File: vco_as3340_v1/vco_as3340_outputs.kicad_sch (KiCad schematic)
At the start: 27 parts, among them J4 TRIANGLE, J5 SAWTOOTH, J6 PULSE, U4 TL072, U5 TL072, U6 TL072, U7 TL072

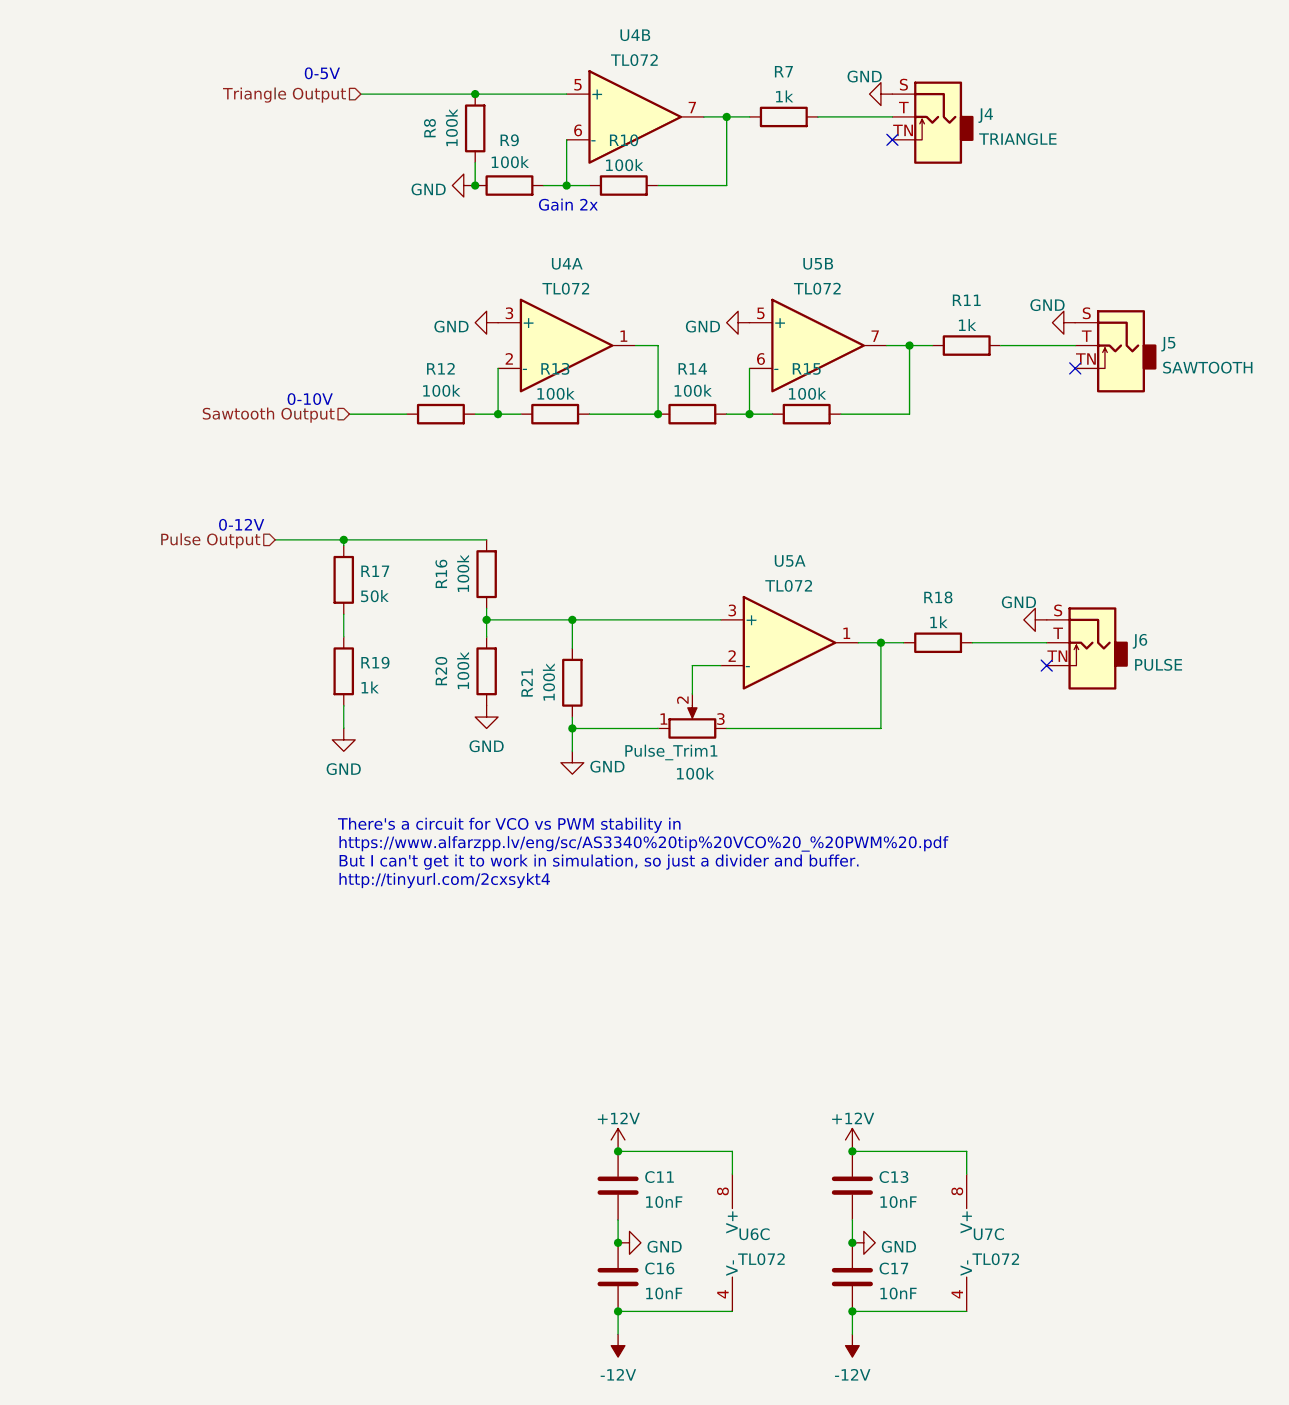
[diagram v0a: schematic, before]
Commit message: Schematic update from breadboarding, start layout
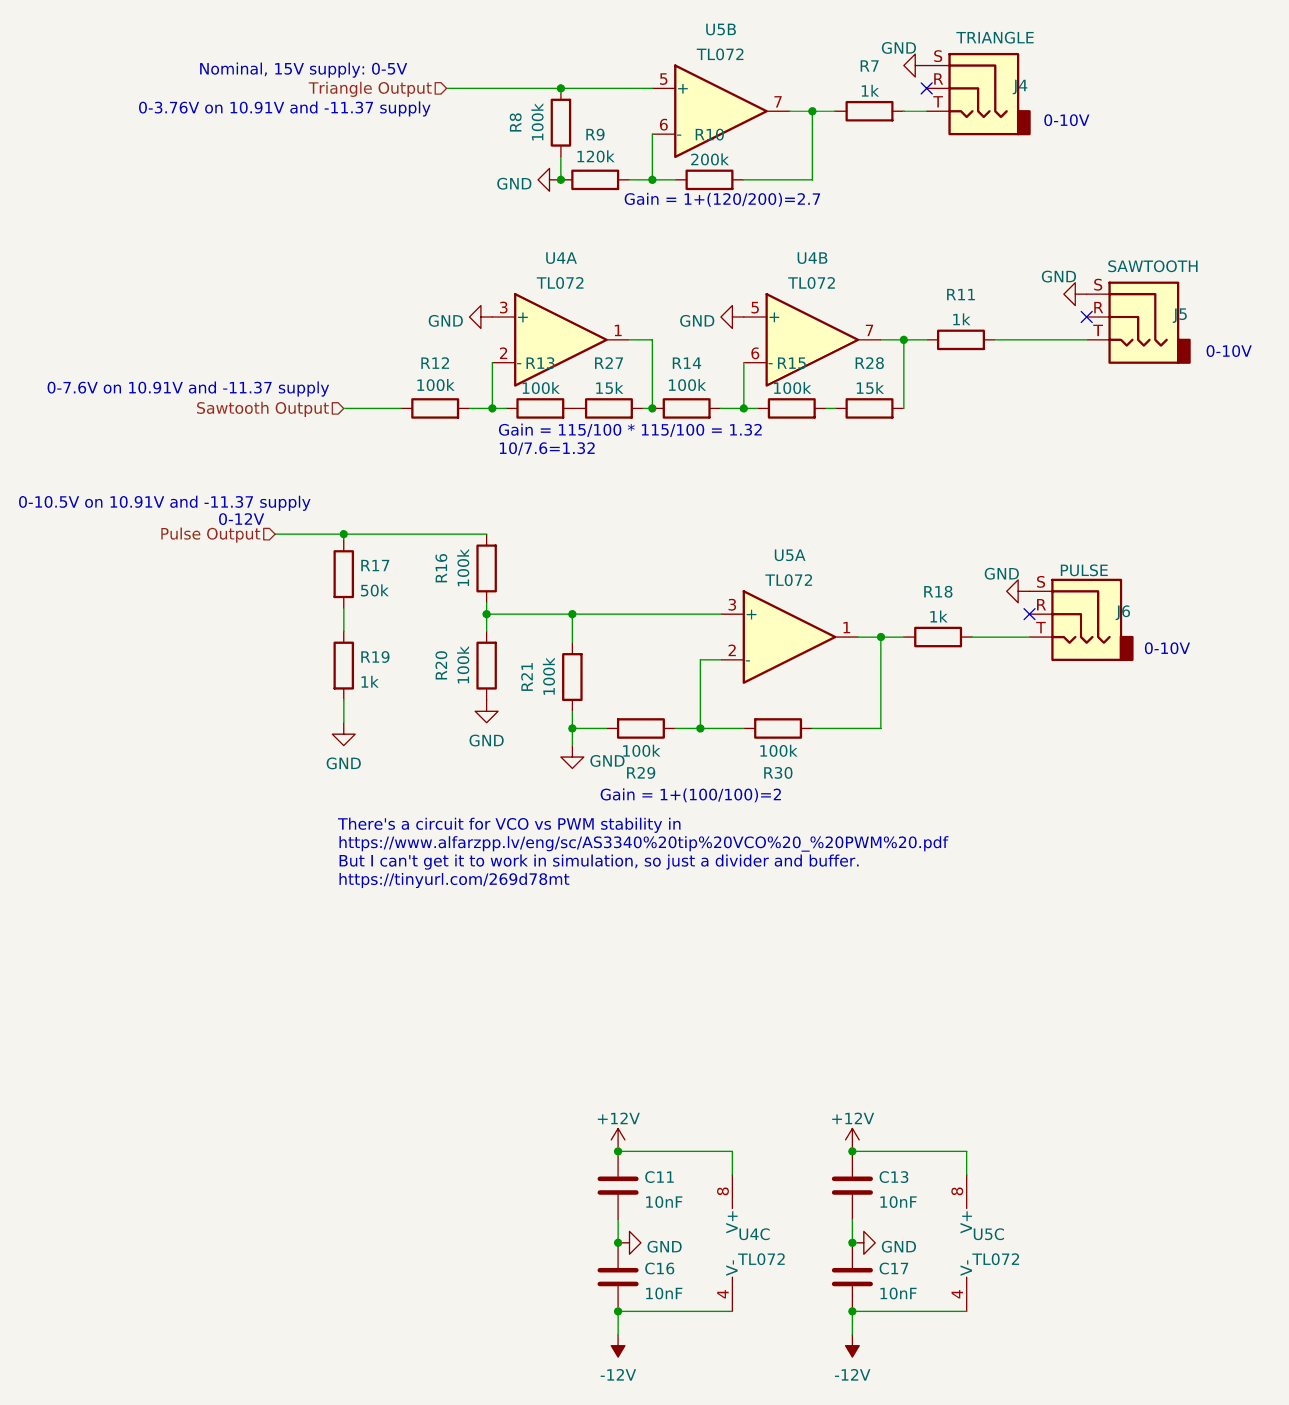
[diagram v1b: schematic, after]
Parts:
- removed Pulse_Trim1: 100k, Potentiometer_THT:Potentiometer_Bourns_3296W_Vertical, symbol Device:R_Potentiometer
- added R27, R28: 15k, Resistor_SMD:R_1206_3216Metric_Pad1.30x1.75mm_HandSolder, symbol Device:R
- added R29, R30: 100k, Resistor_SMD:R_1206_3216Metric_Pad1.30x1.75mm_HandSolder, symbol Device:R
- J4, J5, J6: symbol Connector:AudioJack2_SwitchT -> Connector:AudioJack3
- R10: value 100k -> 200k
- R9: value 100k -> 120k
- renumbered U6 to U4, U5 to U4, U7 to U5, U4 to U5
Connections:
- net GND: now also R29.2
- net at R18.1, U5.1: now also R30.1
- net at R11.1, U4.7: now also R28.2; no longer R15.2
- net at U5.2 (-): now also R29.1, R30.2
- net at R14.1, U4.1: now also R27.2; no longer R13.2
- new net: R13.2, R27.1
- new net: R15.2, R28.1
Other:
- note added: "0-10.5V on 10.91V and -11.37 supply"
- note added: "0-3.76V on 10.91V and -11.37 supply"
- note added: "0-7.6V on 10.91V and -11.37 supply"
- note added: "Gain = 1+(100/100)=2"
- note added: "Gain = 1+(120/200)=2.7"
- note added: "Gain = 115/100 * 115/100 = 1.32 10/7.6=1.32"
- note added: "Nominal, 15V supply: 0-5V"
- note added: "There's a circuit for VCO vs PWM stability in https://www.alfarzpp.lv/eng/sc/AS3340%20tip%20VCO%20_%20PWM%20.pdf But I can't get it to work in simulation, so just a divider and buffer. https://tinyurl.com/269d78mt"
- note removed: "0-5V"
- note removed: "Gain 2x"
- note removed: "There's a circuit for VCO vs PWM stability in https://www.alfarzpp.lv/eng/sc/AS3340%20tip%20VCO%20_%20PWM%20.pdf But I can't get it to work in simulation, so just a divider and buffer. http://tinyurl.com/2cxsykt4"
- moved on the sheet: R10, R11, R12, R13, R14, R15, R16, R17, R18, R19, R20, R21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

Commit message: Geographic re-annotate and cleanup
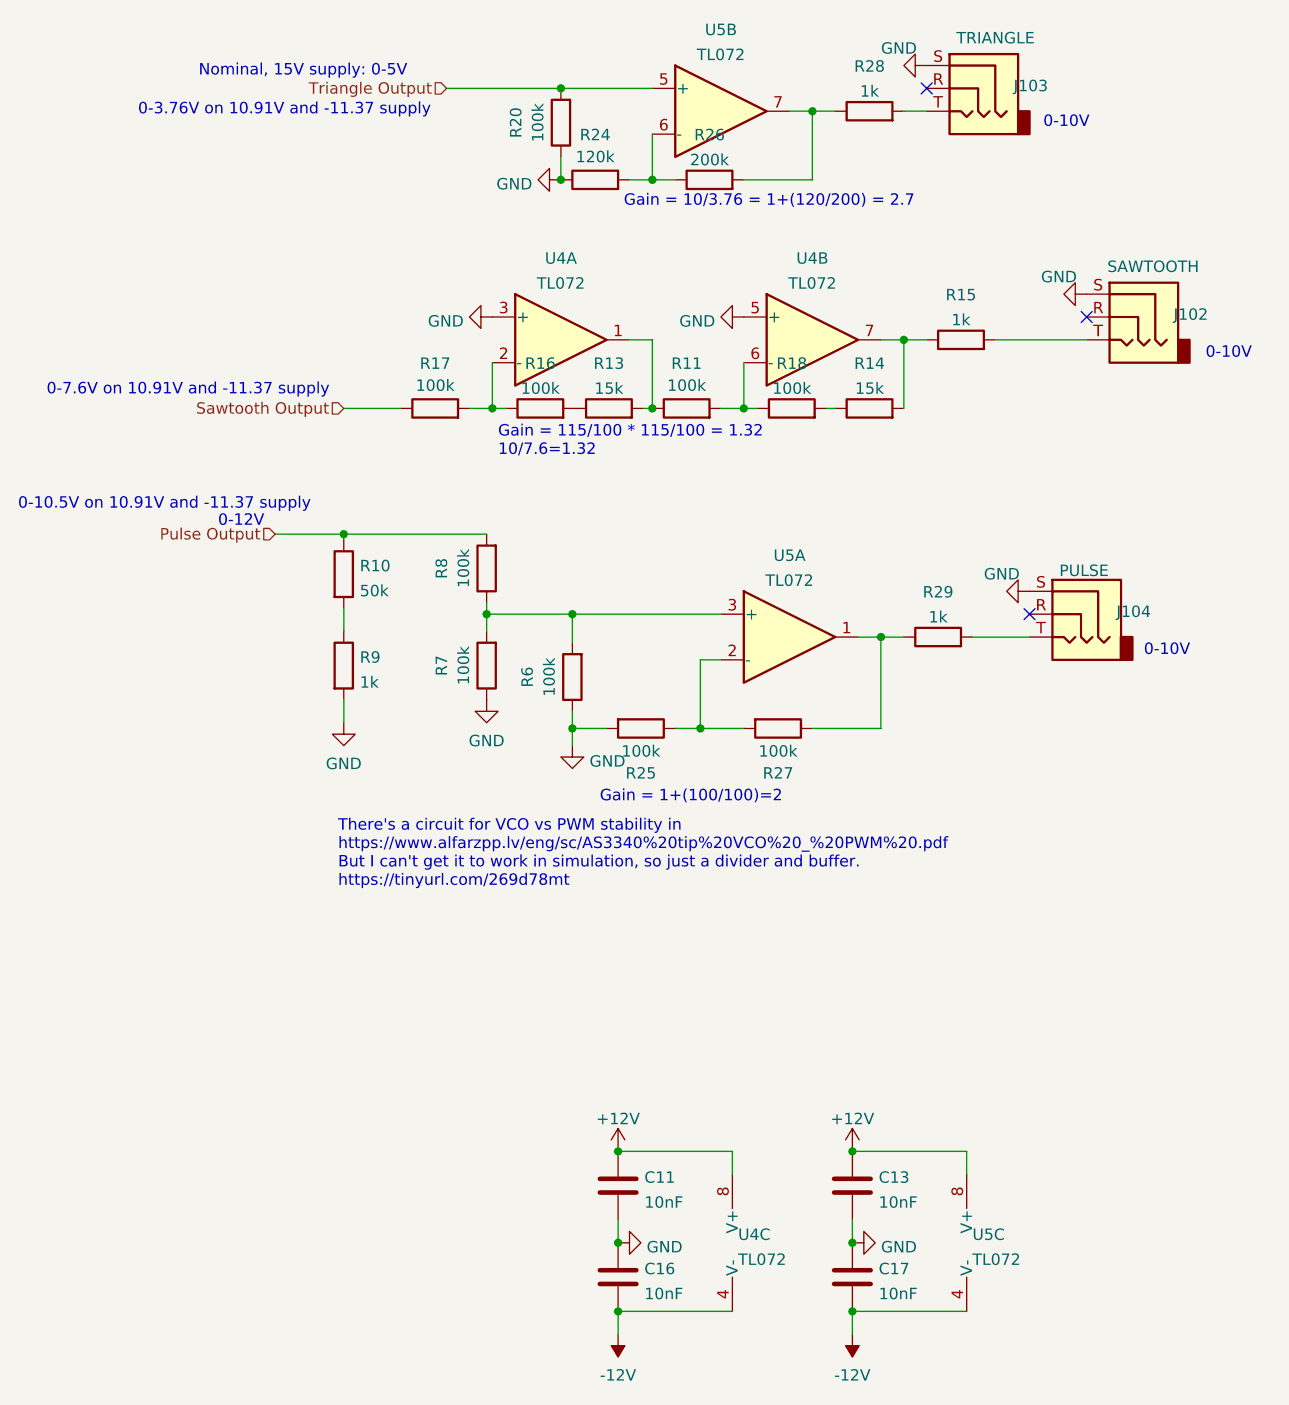
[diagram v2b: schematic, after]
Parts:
- renumbered J5 to J102, J4 to J103, J6 to J104, R17 to R10, R14 to R11, R27 to R13, R28 to R14, R11 to R15, R13 to R16, R12 to R17, R15 to R18, R8 to R20, R9 to R24, R29 to R25, R10 to R26, R30 to R27, R7 to R28, R18 to R29, R21 to R6, R20 to R7, R16 to R8, R19 to R9
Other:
- note added: "Gain = 10/3.76 = 1+(120/200) = 2.7"
- note removed: "Gain = 1+(120/200)=2.7"
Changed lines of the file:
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@@
     (title "3340_VCO")
     (date "2022-07-02")
-    (rev "0.1")
+    (rev "1.0")
     (company "RobotDialogs")
   )
@@
     (effects (font (size 1.27 1.27)) (justify left bottom))
   )
-  (text "Gain = 1+(120/200)=2.7" (at 108.585 36.195 0)
+  (text "Gain = 10/3.76 = 1+(120/200) = 2.7" (at 108.585 36.195 0)
     (effects (font (size 1.27 1.27)) (justify left bottom))
   )
@@
   (symbol (lib_id "Connector:AudioJack3") (at 165.1 48.26 0) (mirror y) (unit 1)
     (in_bom yes) (on_board yes)
-    (property "Reference" "J5" (id 0) (at 169.672 47.9865 0)
+    (property "Reference" "J102" (id 0) (at 169.672 47.9865 0)
       (effects (font (size 1.27 1.27)) (justify right))
     )
@@
   (symbol (lib_id "Device:R") (at 143.51 83.82 90) (unit 1)
     (in_bom yes) (on_board yes) (fields_autoplaced)
-    (property "Reference" "R18" (id 0) (at 143.51 78.8375 90))
+    (property "Reference" "R29" (id 0) (at 143.51 78.8375 90))
     (property "Value" "1k" (id 1) (at 143.51 81.6126 90))
     (property "Footprint" "Resistor_SMD:R_1206_3216Metric_Pad1.30x1.75mm_HandSolder" (id 2) (at 143.51 85.598 90)
@@
   (symbol (lib_id "Device:R") (at 101.6 26.67 180) (unit 1)
     (in_bom yes) (on_board yes)
-    (property "Reference" "R8" (id 0) (at 96.6175 26.67 90))
+    (property "Reference" "R20" (id 0) (at 96.6175 26.67 90))
     (property "Value" "100k" (id 1) (at 99.06 26.67 90))
     (property "Footprint" "Resistor_SMD:R_1206_3216Metric_Pad1.30x1.75mm_HandSolder" (id 2) (at 103.378 26.67 90)
@@
   (symbol (lib_id "Device:R") (at 125.73 93.98 270) (unit 1)
     (in_bom yes) (on_board yes)
-    (property "Reference" "R30" (id 0) (at 125.73 98.9625 90))
+    (property "Reference" "R27" (id 0) (at 125.73 98.9625 90))
     (property "Value" "100k" (id 1) (at 125.73 96.52 90))
     (property "Footprint" "Resistor_SMD:R_1206_3216Metric_Pad1.30x1.75mm_HandSolder" (id 2) (at 125.73 92.202 90)
@@
   (symbol (lib_id "Device:R") (at 106.934 58.42 90) (unit 1)
     (in_bom yes) (on_board yes) (fields_autoplaced)
-    (property "Reference" "R27" (id 0) (at 106.934 53.4375 90))
+    (property "Reference" "R13" (id 0) (at 106.934 53.4375 90))
     (property "Value" "15k" (id 1) (at 106.934 56.2126 90))
     (property "Footprint" "Resistor_SMD:R_1206_3216Metric_Pad1.30x1.75mm_HandSolder" (id 2) (at 106.934 60.198 90)
@@
   (symbol (lib_id "Device:R") (at 146.05 50.8 90) (unit 1)
     (in_bom yes) (on_board yes) (fields_autoplaced)
-    (property "Reference" "R11" (id 0) (at 146.05 45.8175 90))
+    (property "Reference" "R15" (id 0) (at 146.05 45.8175 90))
     (property "Value" "1k" (id 1) (at 146.05 48.5926 90))
     (property "Footprint" "Resistor_SMD:R_1206_3216Metric_Pad1.30x1.75mm_HandSolder" (id 2) (at 146.05 52.578 90)
@@
   (symbol (lib_id "Device:R") (at 135.89 25.4 90) (unit 1)
     (in_bom yes) (on_board yes) (fields_autoplaced)
-    (property "Reference" "R7" (id 0) (at 135.89 20.4175 90))
+    (property "Reference" "R28" (id 0) (at 135.89 20.4175 90))
     (property "Value" "1k" (id 1) (at 135.89 23.1926 90))
     (property "Footprint" "Resistor_SMD:R_1206_3216Metric_Pad1.30x1.75mm_HandSolder" (id 2) (at 135.89 27.178 90)
@@
   (symbol (lib_id "Device:R") (at 110.49 93.98 270) (unit 1)
     (in_bom yes) (on_board yes)
-    (property "Reference" "R29" (id 0) (at 110.49 98.9625 90))
+    (property "Reference" "R25" (id 0) (at 110.49 98.9625 90))
     (property "Value" "100k" (id 1) (at 110.49 96.52 90))
     (property "Footprint" "Resistor_SMD:R_1206_3216Metric_Pad1.30x1.75mm_HandSolder" (id 2) (at 110.49 92.202 90)
@@
   (symbol (lib_id "Device:R") (at 87.63 58.42 90) (unit 1)
     (in_bom yes) (on_board yes)
-    (property "Reference" "R12" (id 0) (at 87.63 53.4375 90))
+    (property "Reference" "R17" (id 0) (at 87.63 53.4375 90))
     (property "Value" "100k" (id 1) (at 87.63 55.88 90))
     (property "Footprint" "Resistor_SMD:R_1206_3216Metric_Pad1.30x1.75mm_HandSolder" (id 2) (at 87.63 60.198 90)
@@
   (symbol (lib_id "Device:R") (at 93.345 76.2 180) (unit 1)
     (in_bom yes) (on_board yes)
-    (property "Reference" "R16" (id 0) (at 88.3625 76.2 90))
+    (property "Reference" "R8" (id 0) (at 88.3625 76.2 90))
     (property "Value" "100k" (id 1) (at 90.805 76.2 90))
     (property "Footprint" "Resistor_SMD:R_1206_3216Metric_Pad1.30x1.75mm_HandSolder" (id 2) (at 95.123 76.2 90)
@@
   (symbol (lib_id "Device:R") (at 105.41 33.02 90) (unit 1)
     (in_bom yes) (on_board yes)
-    (property "Reference" "R9" (id 0) (at 105.41 28.0375 90))
+    (property "Reference" "R24" (id 0) (at 105.41 28.0375 90))
     (property "Value" "120k" (id 1) (at 105.41 30.48 90))
     (property "Footprint" "Resistor_SMD:R_1206_3216Metric_Pad1.30x1.75mm_HandSolder" (id 2) (at 105.41 34.798 90)
@@
   (symbol (lib_id "Device:R") (at 118.11 33.02 90) (unit 1)
     (in_bom yes) (on_board yes) (fields_autoplaced)
-    (property "Reference" "R10" (id 0) (at 118.11 28.0375 90))
+    (property "Reference" "R26" (id 0) (at 118.11 28.0375 90))
     (property "Value" "200k" (id 1) (at 118.11 30.8126 90))
     (property "Footprint" "Resistor_SMD:R_1206_3216Metric_Pad1.30x1.75mm_HandSolder" (id 2) (at 118.11 34.798 90)
@@
   (symbol (lib_id "Connector:AudioJack3") (at 147.32 22.86 0) (mirror y) (unit 1)
     (in_bom yes) (on_board yes)
-    (property "Reference" "J4" (id 0) (at 151.892 22.5865 0)
+    (property "Reference" "J103" (id 0) (at 151.892 22.5865 0)
       (effects (font (size 1.27 1.27)) (justify right))
     )
@@
   (symbol (lib_id "Device:R") (at 115.57 58.42 90) (unit 1)
     (in_bom yes) (on_board yes)
-    (property "Reference" "R14" (id 0) (at 115.57 53.4375 90))
+    (property "Reference" "R11" (id 0) (at 115.57 53.4375 90))
     (property "Value" "100k" (id 1) (at 115.57 55.88 90))
     (property "Footprint" "Resistor_SMD:R_1206_3216Metric_Pad1.30x1.75mm_HandSolder" (id 2) (at 115.57 60.198 90)
@@
   (symbol (lib_id "Device:R") (at 77.47 86.995 0) (unit 1)
     (in_bom yes) (on_board yes) (fields_autoplaced)
-    (property "Reference" "R19" (id 0) (at 79.248 86.0865 0)
+    (property "Reference" "R9" (id 0) (at 79.248 86.0865 0)
       (effects (font (size 1.27 1.27)) (justify left))
     )
@@
   (symbol (lib_id "Connector:AudioJack3") (at 158.75 81.28 0) (mirror y) (unit 1)
     (in_bom yes) (on_board yes)
-    (property "Reference" "J6" (id 0) (at 163.322 81.0065 0)
+    (property "Reference" "J104" (id 0) (at 163.322 81.0065 0)
       (effects (font (size 1.27 1.27)) (justify right))
     )
@@
   (symbol (lib_id "Device:R") (at 93.345 86.995 180) (unit 1)
     (in_bom yes) (on_board yes)
-    (property "Reference" "R20" (id 0) (at 88.3625 86.995 90))
+    (property "Reference" "R7" (id 0) (at 88.3625 86.995 90))
     (property "Value" "100k" (id 1) (at 90.805 86.995 90))
     (property "Footprint" "Resistor_SMD:R_1206_3216Metric_Pad1.30x1.75mm_HandSolder" (id 2) (at 95.123 86.995 90)
@@
   (symbol (lib_id "Device:R") (at 127.254 58.42 90) (unit 1)
     (in_bom yes) (on_board yes) (fields_autoplaced)
-    (property "Reference" "R15" (id 0) (at 127.254 53.4375 90))
+    (property "Reference" "R18" (id 0) (at 127.254 53.4375 90))
     (property "Value" "100k" (id 1) (at 127.254 56.2126 90))
     (property "Footprint" "Resistor_SMD:R_1206_3216Metric_Pad1.30x1.75mm_HandSolder" (id 2) (at 127.254 60.198 90)
@@
   (symbol (lib_id "Device:R") (at 135.89 58.42 90) (unit 1)
     (in_bom yes) (on_board yes) (fields_autoplaced)
-    (property "Reference" "R28" (id 0) (at 135.89 53.4375 90))
+    (property "Reference" "R14" (id 0) (at 135.89 53.4375 90))
     (property "Value" "15k" (id 1) (at 135.89 56.2126 90))
     (property "Footprint" "Resistor_SMD:R_1206_3216Metric_Pad1.30x1.75mm_HandSolder" (id 2) (at 135.89 60.198 90)
@@
   (symbol (lib_id "Device:R") (at 99.314 58.42 90) (unit 1)
     (in_bom yes) (on_board yes) (fields_autoplaced)
-    (property "Reference" "R13" (id 0) (at 99.314 53.4375 90))
+    (property "Reference" "R16" (id 0) (at 99.314 53.4375 90))
     (property "Value" "100k" (id 1) (at 99.314 56.2126 90))
     (property "Footprint" "Resistor_SMD:R_1206_3216Metric_Pad1.30x1.75mm_HandSolder" (id 2) (at 99.314 60.198 90)
@@
   (symbol (lib_id "Device:R") (at 102.87 88.265 180) (unit 1)
     (in_bom yes) (on_board yes)
-    (property "Reference" "R21" (id 0) (at 97.8875 88.265 90))
+    (property "Reference" "R6" (id 0) (at 97.8875 88.265 90))
     (property "Value" "100k" (id 1) (at 100.33 88.265 90))
     (property "Footprint" "Resistor_SMD:R_1206_3216Metric_Pad1.30x1.75mm_HandSolder" (id 2) (at 104.648 88.265 90)
@@
   (symbol (lib_id "Device:R") (at 77.47 76.835 0) (unit 1)
     (in_bom yes) (on_board yes) (fields_autoplaced)
-    (property "Reference" "R17" (id 0) (at 79.248 75.9265 0)
-      (effects (font (size 1.27 1.27)) (justify left))
-    )
+    (property "Reference" "R10" (id 0) (at 79.248 75.9265 0)
+      (effects (font (size 1.27 1.27)) (justify left))
+    )
